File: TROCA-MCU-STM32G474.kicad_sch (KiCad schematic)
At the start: 19 parts, among them SW1 HX-3X6X2.5-X SMD TACT SWITCH, SW2 HX-3X6X2.5-X SMD TACT SWITCH, U3 STM32G474VETx, X1 X32258MOB4SI

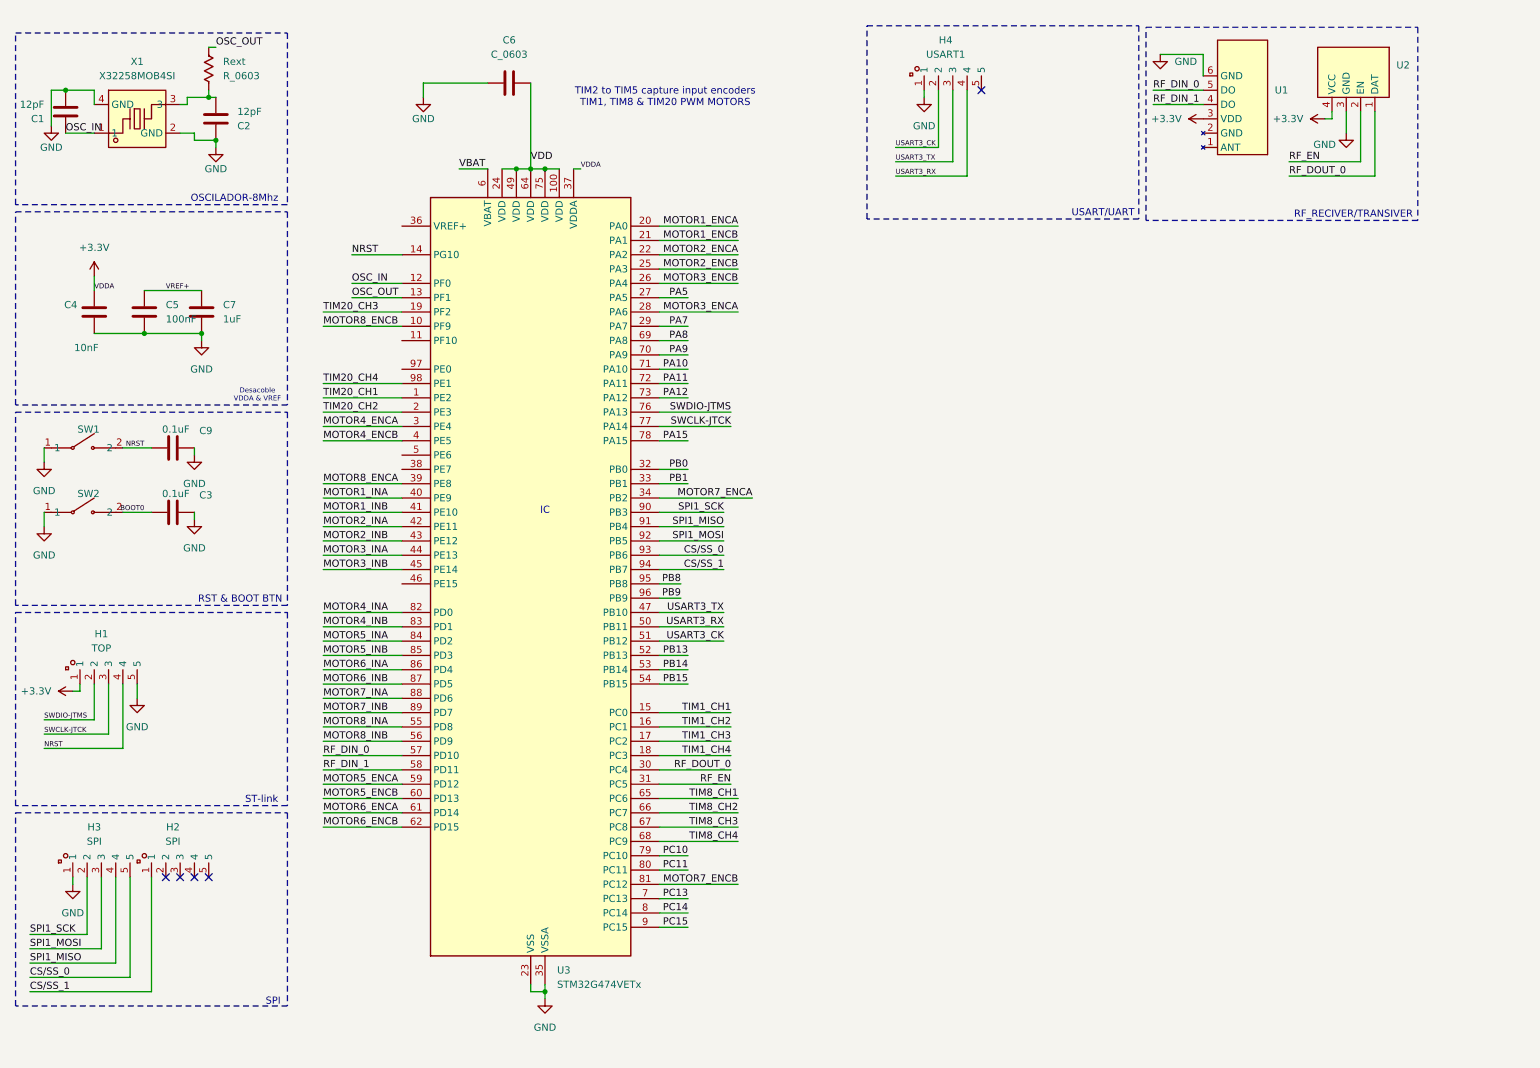
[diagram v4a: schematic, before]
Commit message: asignacion de pines terminado
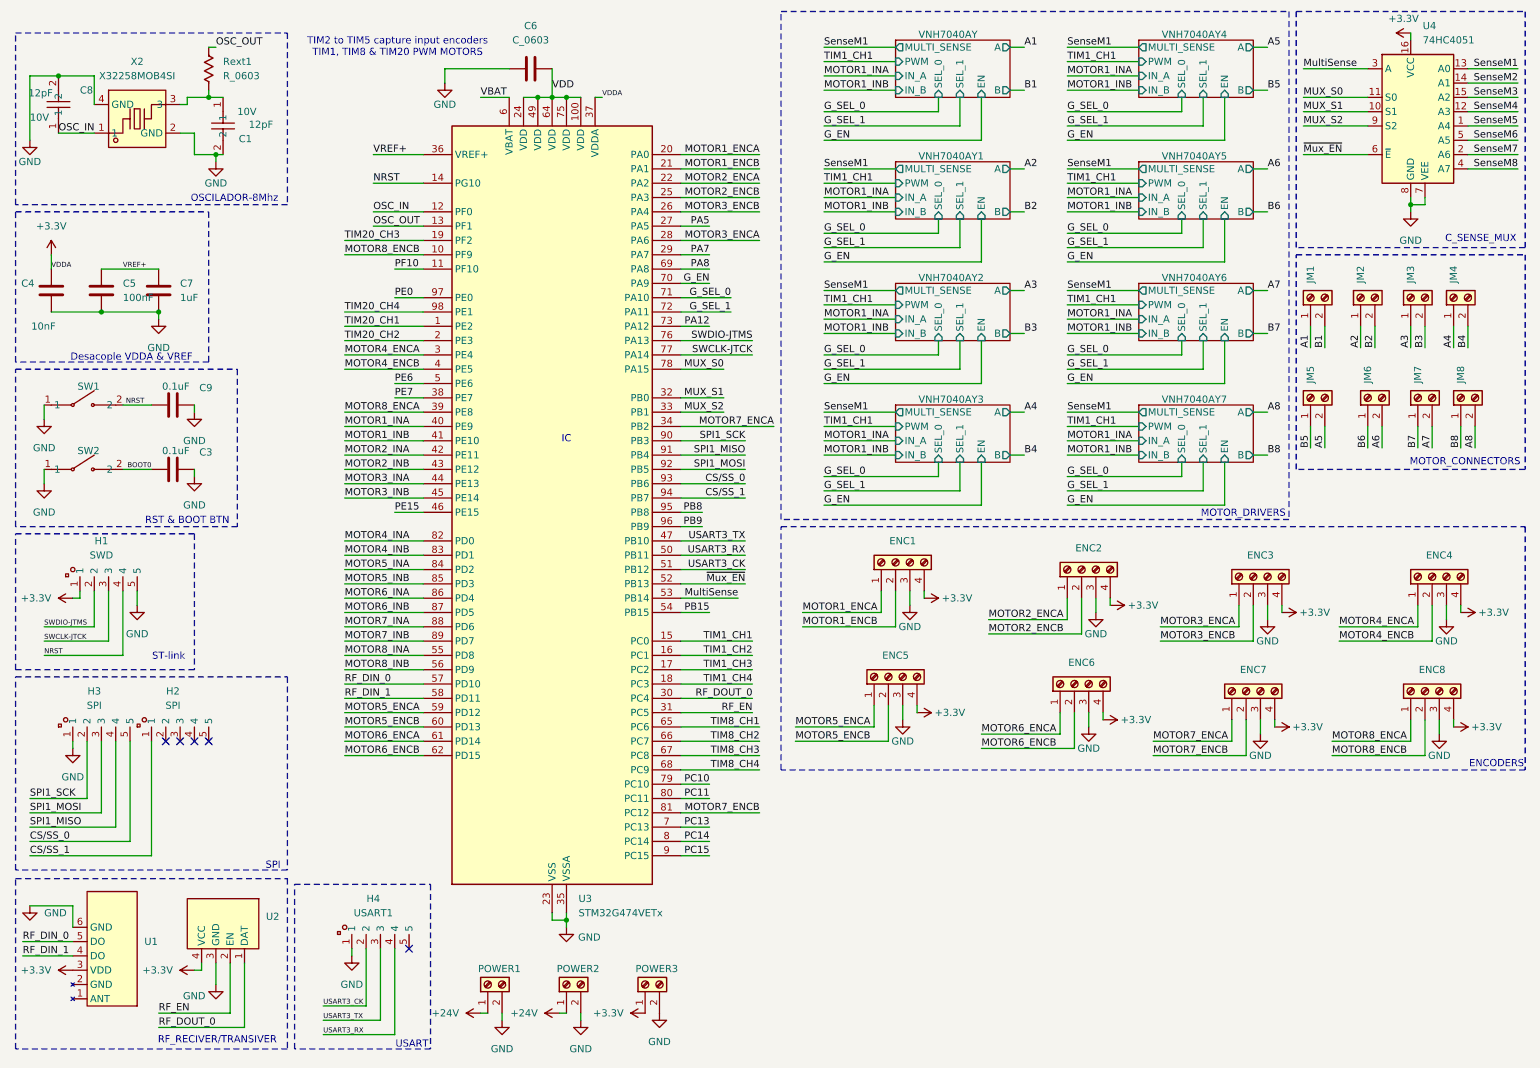
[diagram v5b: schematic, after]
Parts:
- removed C1, C2: 12pF, symbol Device:C
- removed X1: X32258MOB4SI, EasyEDA:CRYSTAL-SMD_4P-L3.2-W2.5-BL, symbol EasyEDA:X32258MOB4SI
- added C1, C8: 12pF, EasyEDA:C0603, symbol EasyEDA:VJ0603A120FXQCW1BC
- added ENC1, ENC2, ENC3, ENC4, ENC5, ENC6, ENC7, ENC8: Screw_Terminal_01x04, TerminalBlock:TerminalBlock_Xinya_XY308-2.54-4P_1x04_P2.54mm_Horizontal, symbol Connector:Screw_Terminal_01x04
- added JM1, JM2, JM3, JM4, JM5, JM6, JM7, JM8, POWER1, POWER2, POWER3: Screw_Terminal_01x02, TerminalBlock:TerminalBlock_Xinya_XY308-2.54-2P_1x02_P2.54mm_Horizontal, symbol Connector:Screw_Terminal_01x02
- added U4: 74HC4051, EasyEDA:PDIP-16_L19.3-W6.4-P2.54-LS7.94-BL, symbol 74xx:74HC4051
- added X2: X32258MOB4SI, EasyEDA:CRYSTAL-SMD_4P-L3.2-W2.5-BL, symbol EasyEDA:X32258MOB4SI
- H1: value TOP -> SWD
- U1: footprint (none) -> PCM_rf_433MHz_receiver_print:rf_433mhz_receiver
- U2: footprint (none) -> PCM_rf_433MHz_receiver_print:RF_433MHz_transmisor
- renumbered Rext to Rext1
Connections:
- net +3.3V: now also ENC1.4 (Pin_4), ENC2.4 (Pin_4), ENC3.4 (Pin_4), ENC4.4 (Pin_4), ENC5.4 (Pin_4), ENC6.4 (Pin_4), ENC7.4 (Pin_4), ENC8.4 (Pin_4), POWER3.1 (Pin_1), U4.16 (VCC)
- net GND: now also C1.2, C8.2, ENC1.3 (Pin_3), ENC2.3 (Pin_3), ENC3.3 (Pin_3), ENC4.3 (Pin_3), ENC5.3 (Pin_3), ENC6.3 (Pin_3), ENC7.3 (Pin_3), ENC8.3 (Pin_3), POWER1.2 (Pin_2), POWER2.2 (Pin_2), POWER3.2 (Pin_2), U4.7 (VEE), U4.8 (GND), X2.2 (GND), X2.4 (GND)
- net MOTOR1_ENCA: now also ENC1.1 (Pin_1)
- net MOTOR1_ENCB: now also ENC1.2 (Pin_2)
- net MOTOR2_ENCA: now also ENC2.1 (Pin_1)
- net MOTOR2_ENCB: now also ENC2.2 (Pin_2)
- net MOTOR3_ENCA: now also ENC3.1 (Pin_1)
- net MOTOR3_ENCB: now also ENC3.2 (Pin_2)
- net MOTOR4_ENCA: now also ENC4.1 (Pin_1)
- net MOTOR4_ENCB: now also ENC4.2 (Pin_2)
- net MOTOR5_ENCA: now also ENC5.1 (Pin_1)
- net MOTOR5_ENCB: now also ENC5.2 (Pin_2)
- net MOTOR6_ENCA: now also ENC6.1 (Pin_1)
- net MOTOR6_ENCB: now also ENC6.2 (Pin_2)
- net MOTOR7_ENCA: now also ENC7.1 (Pin_1)
- net MOTOR7_ENCB: now also ENC7.2 (Pin_2)
- net MOTOR8_ENCA: now also ENC8.1 (Pin_1)
- net MOTOR8_ENCB: now also ENC8.2 (Pin_2)
- net OSC_IN: now also C8.1, X2.1
- net VREF+: now also U3.36 (VREF+)
- net PF10: now reaches U3.11 (PF10)
- net PE7: now reaches U3.38 (PE7)
- net PE15: now reaches U3.46 (PE15)
- net PE6: now reaches U3.5 (PE6)
- net PE0: now reaches U3.97 (PE0)
- net at Rext1.1: now also C1.1, X2.3
- net PA10 renamed G_SEL_0
- net PA11 renamed G_SEL_1
- net PA15 renamed MUX_S0
- net MUX_S0: now also U4.11 (S0)
- net PA9 renamed G_EN
- net PB0 renamed MUX_S1
- net MUX_S1: now also U4.10 (S1)
- net PB1 renamed MUX_S2
- net MUX_S2: now also U4.9 (S2)
- net PB13 renamed ~{Mux_EN}
- net ~{Mux_EN}: now also U4.6 (~{E})
- net PB14 renamed MultiSense
- net MultiSense: now also U4.3 (A)
- new net +24V: POWER1.1 (Pin_1), POWER2.1 (Pin_1)
- new net A1: JM1.1 (Pin_1)
- new net A2: JM2.1 (Pin_1)
- new net A3: JM3.1 (Pin_1)
- new net A4: JM4.1 (Pin_1)
- new net A5: JM5.2 (Pin_2)
- new net A6: JM6.2 (Pin_2)
- new net A7: JM7.2 (Pin_2)
- new net A8: JM8.2 (Pin_2)
- new net B1: JM1.2 (Pin_2)
- new net B2: JM2.2 (Pin_2)
- new net B3: JM3.2 (Pin_2)
- new net B4: JM4.2 (Pin_2)
- new net B5: JM5.1 (Pin_1)
- new net B6: JM6.1 (Pin_1)
- new net B7: JM7.1 (Pin_1)
- new net B8: JM8.1 (Pin_1)
- new net SenseM1: U4.13 (A0)
- new net SenseM2: U4.14 (A1)
- new net SenseM3: U4.15 (A2)
- new net SenseM4: U4.12 (A3)
- new net SenseM5: U4.1 (A4)
- new net SenseM6: U4.5 (A5)
- new net SenseM7: U4.2 (A6)
- new net SenseM8: U4.4 (A7)
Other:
- added sheet VNH7040AY (Motor_Driver.kicad_sch)
- added sheet VNH7040AY1 (Motor_Driver.kicad_sch)
- added sheet VNH7040AY2 (Motor_Driver.kicad_sch)
- added sheet VNH7040AY3 (Motor_Driver.kicad_sch)
- added sheet VNH7040AY4 (Motor_Driver.kicad_sch)
- added sheet VNH7040AY5 (Motor_Driver.kicad_sch)
- added sheet VNH7040AY6 (Motor_Driver.kicad_sch)
- added sheet VNH7040AY7 (Motor_Driver.kicad_sch)
- note added: "C_SENSE_MUX"
- note added: "Desacople VDDA & VREF"
- note added: "ENCODERS"
- note added: "MOTOR_CONNECTORS"
- note added: "MOTOR_DRIVERS"
- note added: "USART"
- note removed: "Desacoble VDDA & VREF"
- note removed: "USART/UART"
- moved on the sheet: C3, C4, C5, C6, C7, C9, H1, H2, H3, H4, SW1, SW2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
